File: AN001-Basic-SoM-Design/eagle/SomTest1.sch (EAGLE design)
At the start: 42 parts, among them J1 SPARK_M.2EKEY, U1 MAX17043, U2 BQ24195, U3 XCL223

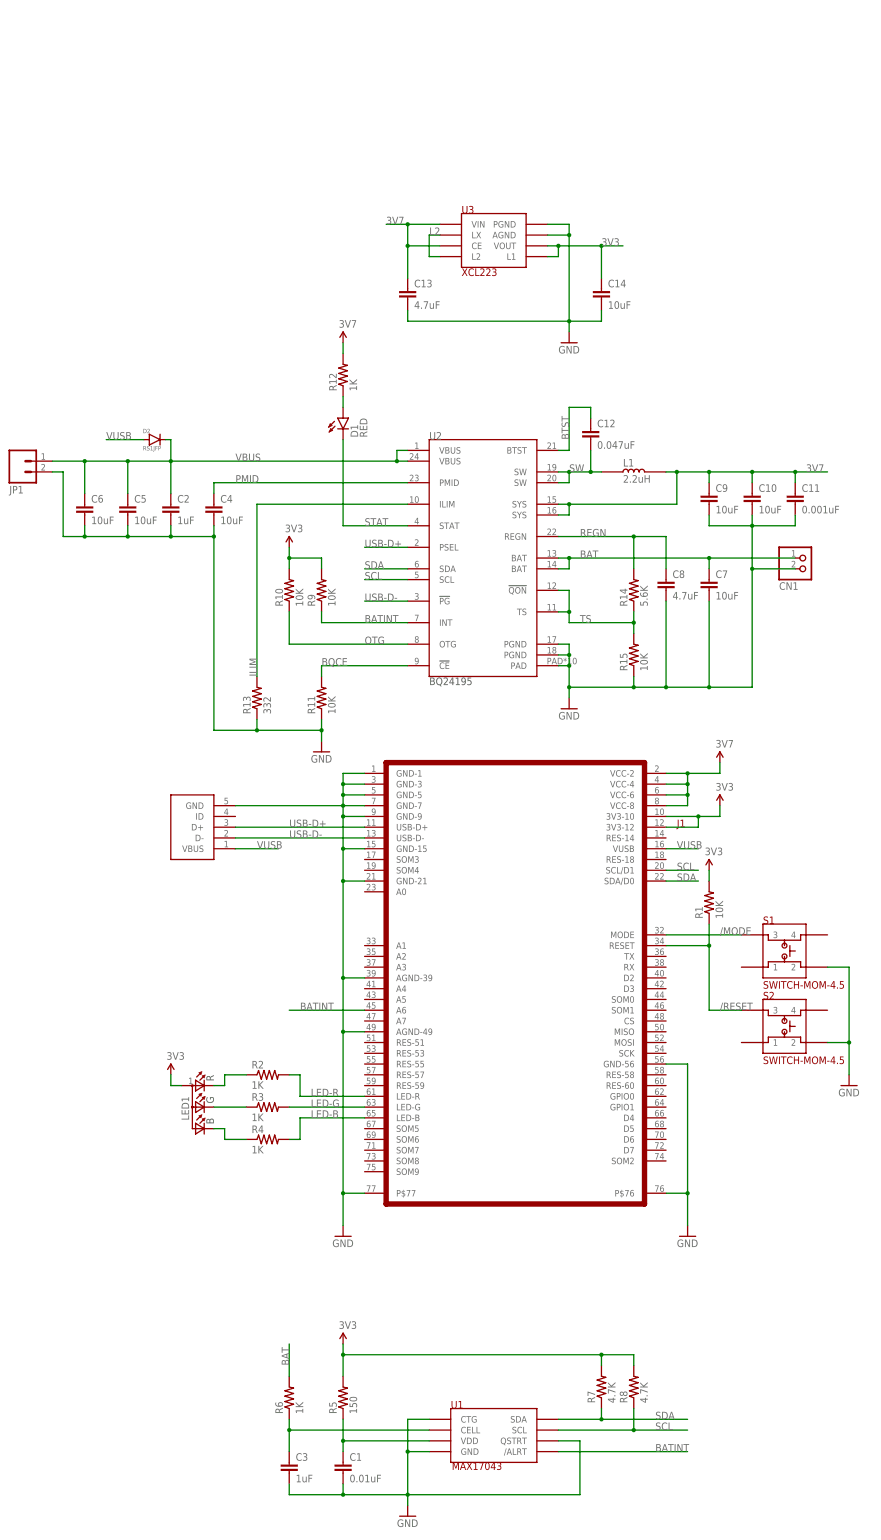
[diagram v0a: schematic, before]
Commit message: Update M.2 standoff
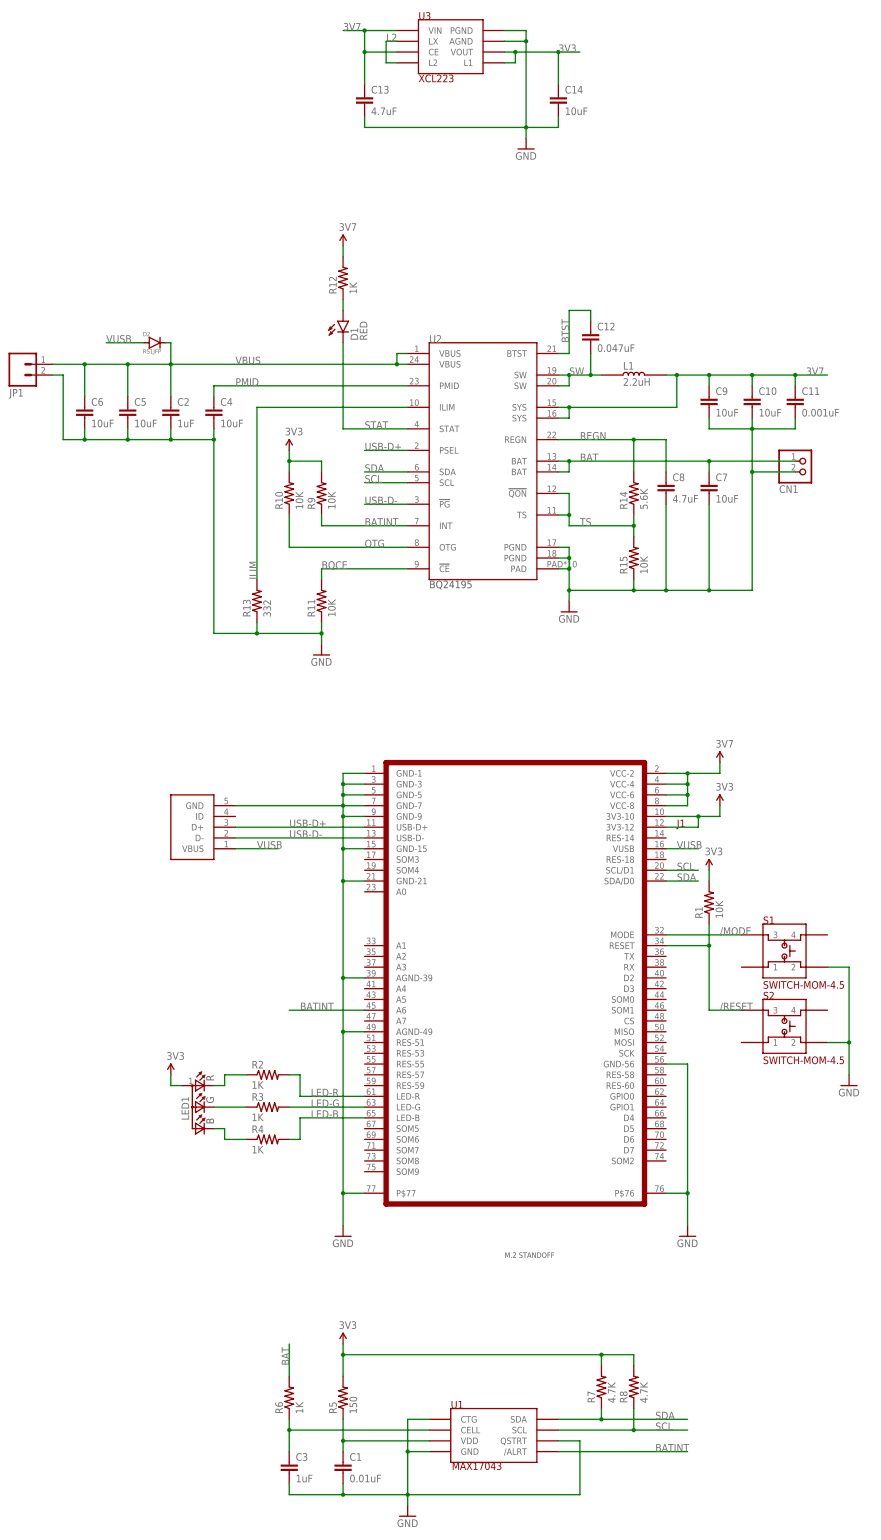
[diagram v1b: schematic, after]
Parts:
- added U$1: M2-STANDOFF, rickk2:M2-STANDOFF
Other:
- moved on the sheet: C10, C11, C12, C13, C14, C2, C4, C5, C6, C7, C8, C9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
